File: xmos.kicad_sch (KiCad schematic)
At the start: 83 parts, among them J4 XTAG JTAG (xSYS2 pins 1-10), Q1 LBSS138WT1G, Q2 LBSS138WT1G, Q3 BC847B, U10 XU316-1024-QF60B-C24​, U11 W25Q32JVSSIQ, U12 SN74LVC125APWR, U13 TLV73333PDBVR, X1 24MHz 12pF

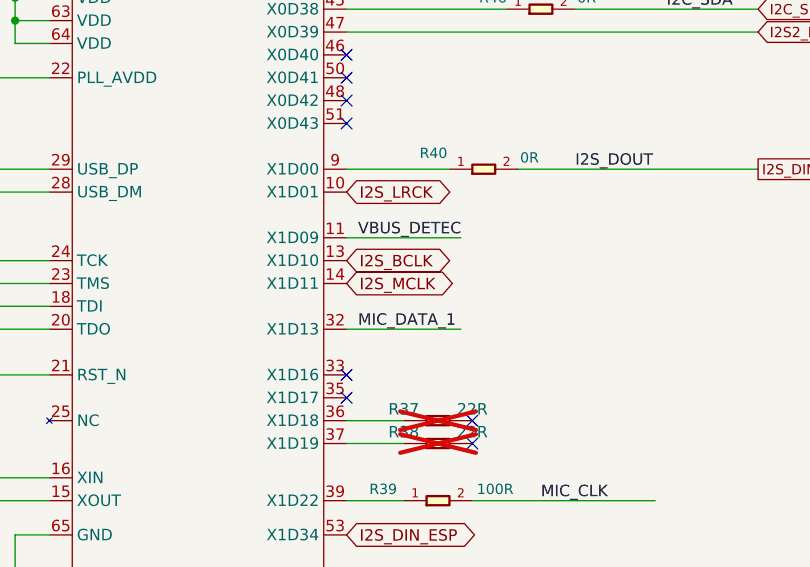
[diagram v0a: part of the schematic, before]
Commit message: v2.1: octilinear re-route of added tracks, bundled JTAG, TI-style buck layout, v2.1 silkscreen
All tracks added in v2-fix re-routed at 0/45/90 deg with no mid-trace splits; branches only at pads or vias. JTAG runs as one parallel bundle (J4 moved to the top side). Buck converter re-laid with power polygons. XU316_RST moved to GPIO21, LED data to GPIO4, X1D11 MCLK left unconnected; MiciMike.yaml updated to match. Silkscreen and title blocks now say v2.1. KiCad 9 DRC with schematic parity shows only the items already on the v2 board. See CHANGES-v2fix.md.

Co-Authored-By: Claude Opus 5.5 <noreply@anthropic.com>
Claude-Session: https://claude.ai/code/session_01DBYfebaHp5UuC2Xws8yAJw
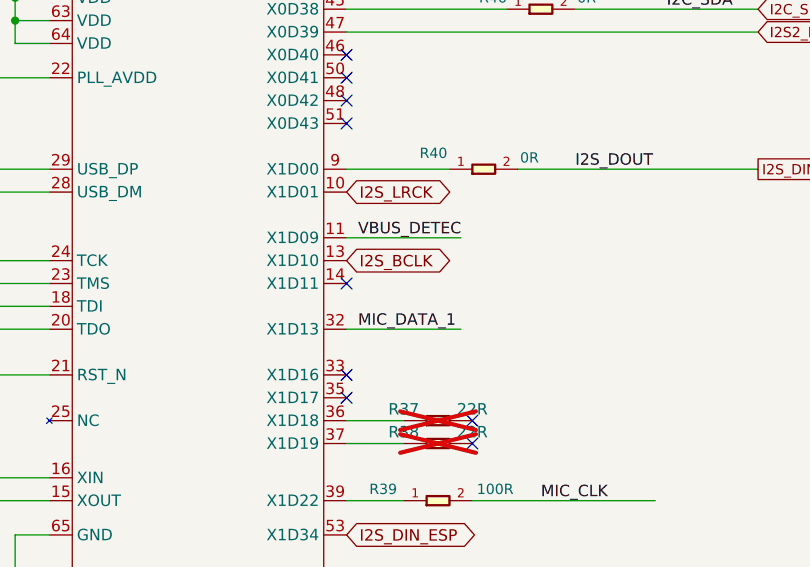
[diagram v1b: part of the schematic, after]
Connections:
- net I2S_MCLK: no longer names the net of U10.14 (X1D11)
- no-connect marks 12 -> 13
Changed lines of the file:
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@@
 	(title_block
 		(title "Drop in replacement PCB for Nest mini GEN2")
-		(rev "v1")
+		(rev "v2.1")
 		(company "by iMike78 (inpired by Onju voice and HA VPE)")
 	)
@@
 		(property "Intersheetrefs" "${INTERSHEET_REFS}" (at 152.4 149.86 0) (effects (font (size 1.27 1.27)) (hide yes)))
 	)
-	(global_label "I2S_MCLK"
-		(shape bidirectional)
-		(at 152.4 121.92 0)
-		(fields_autoplaced yes)
-		(effects (font (size 1.27 1.27)) (justify left))
-		(property "Intersheetrefs" "${INTERSHEET_REFS}" (at 152.4 121.92 0) (effects (font (size 1.27 1.27)) (hide yes)))
-	)
+	(no_connect (at 152.4 121.92))
 	(label "MIC_DATA_M_2" (at 289.56 78.74 0) (fields_autoplaced yes) (effects (font (size 1.27 1.27)) (justify left bottom)))
 	(wire (pts (xy 322.58 83.82) (xy 317.5 83.82)) (stroke (width 0) (type default)))
